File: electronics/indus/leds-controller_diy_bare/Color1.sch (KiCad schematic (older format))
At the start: 17 parts

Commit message: wip bare diy controller - dcdc and refactor
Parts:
- gave numbers to parts that had none: 17
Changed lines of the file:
@@
 $Descr A4 11693 8268
 encoding utf-8
-Sheet 4 8
+Sheet 4 9
 Title "Carte controlleur de LEDs 4 canaux"
 Date ""
@@
 VIN
 $Comp
-L TPS92513 U?
+L TPS92513 U4
 U 1 1 57155637
 P 5800 3550
-F 0 "U?" H 6150 2600 60  0000 C CNN
+F 0 "U4" H 6150 2600 60  0000 C CNN
 F 1 "TPS92513" H 5400 2600 60  0000 C CNN
 F 2 "" H 5950 3650 60  0000 C CNN
@@
 $EndComp
 $Comp
-L C-RESCUE-leds-controller C?
+L C-RESCUE-leds-controller C14
 U 1 1 5715571A
 P 1600 4150
-F 0 "C?" H 1600 4250 40  0000 L CNN
+F 0 "C14" H 1600 4250 40  0000 L CNN
 F 1 "C" H 1606 4065 40  0000 L CNN
 F 2 "" H 1638 4000 30  0000 C CNN
@@
 $EndComp
 $Comp
-L GND-RESCUE-leds-controller #PWR?
+L GND-RESCUE-leds-controller #PWR019
 U 1 1 571557B2
 P 5950 5250
-F 0 "#PWR?" H 5950 5250 30  0001 C CNN
+F 0 "#PWR019" H 5950 5250 30  0001 C CNN
 F 1 "GND" H 5950 5180 30  0001 C CNN
 F 2 "" H 5950 5250 60  0000 C CNN
@@
 $EndComp
 $Comp
-L R-RESCUE-leds-controller R?
+L R-RESCUE-leds-controller R15
 U 1 1 571557E1
 P 2150 3800
-F 0 "R?" V 2230 3800 40  0000 C CNN
+F 0 "R15" V 2230 3800 40  0000 C CNN
 F 1 "R" V 2157 3801 40  0000 C CNN
 F 2 "" V 2080 3800 30  0000 C CNN
@@
 $EndComp
 $Comp
-L R-RESCUE-leds-controller R?
+L R-RESCUE-leds-controller R16
 U 1 1 5715580E
 P 2150 4500
-F 0 "R?" V 2230 4500 40  0000 C CNN
+F 0 "R16" V 2230 4500 40  0000 C CNN
 F 1 "R" V 2157 4501 40  0000 C CNN
 F 2 "" V 2080 4500 30  0000 C CNN
@@
 $EndComp
 $Comp
-L C-RESCUE-leds-controller C?
+L C-RESCUE-leds-controller C15
 U 1 1 5715589F
 P 3050 4300
-F 0 "C?" H 3050 4400 40  0000 L CNN
+F 0 "C15" H 3050 4400 40  0000 L CNN
 F 1 "C" H 3056 4215 40  0000 L CNN
 F 2 "" H 3088 4150 30  0000 C CNN
@@
 $EndComp
 $Comp
-L R-RESCUE-leds-controller R?
+L R-RESCUE-leds-controller R17
 U 1 1 571558C4
 P 4050 4500
-F 0 "R?" V 4130 4500 40  0000 C CNN
+F 0 "R17" V 4130 4500 40  0000 C CNN
 F 1 "R" V 4057 4501 40  0000 C CNN
 F 2 "" V 3980 4500 30  0000 C CNN
@@
 $EndComp
 $Comp
-L INDUCTOR L?
+L INDUCTOR L3
 U 1 1 57155F0C
 P 8200 3450
-F 0 "L?" V 8150 3450 40  0000 C CNN
+F 0 "L3" V 8150 3450 40  0000 C CNN
 F 1 "XAL6060-153MEC - 15µH - 6A" V 8300 3450 40  0000 C CNN
 F 2 "risebox:SELF_COILCRAFT_XAL6060-153" H 8200 3450 60  0001 C CNN
@@
 self métallique
 $Comp
-L C-RESCUE-leds-controller C?
+L C-RESCUE-leds-controller C16
 U 1 1 571560D6
 P 6800 2900
-F 0 "C?" H 6800 3000 40  0000 L CNN
+F 0 "C16" H 6800 3000 40  0000 L CNN
 F 1 "C" H 6806 2815 40  0000 L CNN
 F 2 "" H 6838 2750 30  0000 C CNN
@@
 $EndComp
 $Comp
-L C-RESCUE-leds-controller C?
+L C-RESCUE-leds-controller C17
 U 1 1 57156549
 P 9550 3750
-F 0 "C?" H 9550 3850 40  0000 L CNN
+F 0 "C17" H 9550 3850 40  0000 L CNN
 F 1 "C" H 9556 3665 40  0000 L CNN
 F 2 "" H 9588 3600 30  0000 C CNN
@@
 $EndComp
 $Comp
-L R-RESCUE-leds-controller R?
+L R-RESCUE-leds-controller R18
 U 1 1 5715662A
 P 8200 4050
-F 0 "R?" V 8280 4050 40  0000 C CNN
+F 0 "R18" V 8280 4050 40  0000 C CNN
 F 1 "R" V 8207 4051 40  0000 C CNN
 F 2 "" V 8130 4050 30  0000 C CNN
@@
 $EndComp
 $Comp
-L R-RESCUE-leds-controller R?
+L R-RESCUE-leds-controller R19
 U 1 1 57156725
 P 10150 4500
-F 0 "R?" V 10230 4500 40  0000 C CNN
+F 0 "R19" V 10230 4500 40  0000 C CNN
 F 1 "R" V 10157 4501 40  0000 C CNN
 F 2 "" V 10080 4500 30  0000 C CNN
@@
 $EndComp
 $Comp
-L DIODESCH D?
+L DIODESCH D4
 U 1 1 57156848
 P 7350 4500
-F 0 "D?" H 7350 4600 40  0000 C CNN
+F 0 "D4" H 7350 4600 40  0000 C CNN
 F 1 "DIODESCH" H 7350 4400 40  0000 C CNN
 F 2 "" H 7350 4500 60  0000 C CNN
@@
 PDIM
 $Comp
-L JUMPER JP?
+L JUMPER JP1
 U 1 1 5760B831
 P 2400 1000
-F 0 "JP?" H 2400 1150 50  0000 C CNN
+F 0 "JP1" H 2400 1150 50  0000 C CNN
 F 1 "JUMPER" H 2400 920 50  0000 C CNN
 F 2 "" H 2400 1000 50  0000 C CNN
@@
 $EndComp
 $Comp
-L JUMPER JP?
+L JUMPER JP2
 U 1 1 5760B8E2
 P 2400 1350
-F 0 "JP?" H 2400 1500 50  0000 C CNN
+F 0 "JP2" H 2400 1500 50  0000 C CNN
 F 1 "JUMPER" H 2400 1270 50  0000 C CNN
 F 2 "" H 2400 1350 50  0000 C CNN
@@
 $EndComp
 $Comp
-L JUMPER JP?
+L JUMPER JP3
 U 1 1 5760B931
 P 2400 1700
-F 0 "JP?" H 2400 1850 50  0000 C CNN
+F 0 "JP3" H 2400 1850 50  0000 C CNN
 F 1 "JUMPER" H 2400 1620 50  0000 C CNN
 F 2 "" H 2400 1700 50  0000 C CNN
@@
 $EndComp
 $Comp
-L JUMPER JP?
+L JUMPER JP4
 U 1 1 5760B986
 P 2400 2050
-F 0 "JP?" H 2400 2200 50  0000 C CNN
+F 0 "JP4" H 2400 2200 50  0000 C CNN
 F 1 "JUMPER" H 2400 1970 50  0000 C CNN
 F 2 "" H 2400 2050 50  0000 C CNN
@@
 REG_0.35A
 $Comp
-L JUMPER JP?
+L JUMPER JP5
 U 1 1 5760BC5B
 P 5650 1450
-F 0 "JP?" H 5650 1600 50  0000 C CNN
+F 0 "JP5" H 5650 1600 50  0000 C CNN
 F 1 "JUMPER" H 5650 1370 50  0000 C CNN
 F 2 "" H 5650 1450 50  0000 C CNN

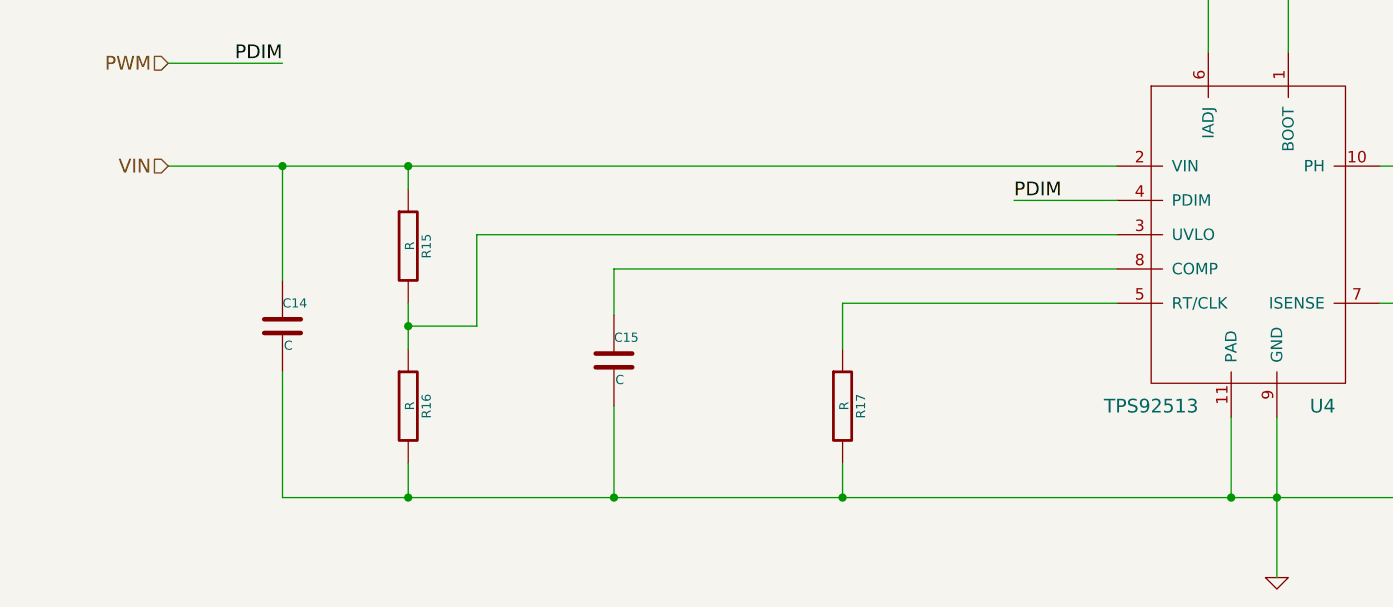
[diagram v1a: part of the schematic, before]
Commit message: schema done - misses values
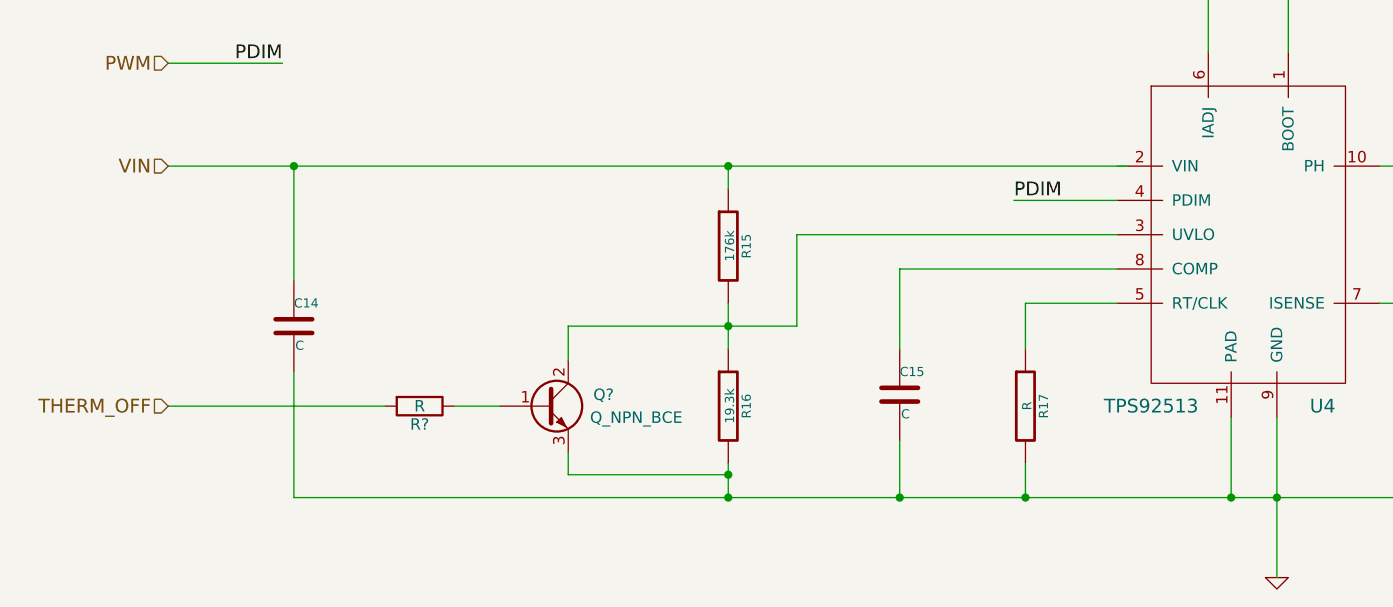
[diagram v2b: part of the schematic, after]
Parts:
- added Q?: Q_NPN_BCE, symbol Q_NPN_BCE
- added R?: R, symbol R
- R15: value R -> 176k
- R16: value R -> 19.3k
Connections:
- net GND: now also Q?.3 (E)
- net VIN: no longer U4.2 (VIN)
- net at R15.2, R16.1, U4.3 (UVLO): now also Q?.2 (C)
- new net: Q?.1 (B), R?.1
- new net THERM_OFF: R?.2
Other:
- moved on the sheet: C14, C15, R15, R16, R17
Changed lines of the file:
@@
 $Descr A4 11693 8268
 encoding utf-8
-Sheet 4 9
+Sheet 3 9
 Title "Carte controlleur de LEDs 4 canaux"
 Date ""
@@
 L C-RESCUE-leds-controller C14
 U 1 1 5715571A
-P 1600 4150
-F 0 "C14" H 1600 4250 40  0000 L CNN
-F 1 "C" H 1606 4065 40  0000 L CNN
-F 2 "" H 1638 4000 30  0000 C CNN
-F 3 "" H 1600 4150 60  0000 C CNN
-	1    1600 4150
+P 1650 4150
+F 0 "C14" H 1650 4250 40  0000 L CNN
+F 1 "C" H 1656 4065 40  0000 L CNN
+F 2 "" H 1688 4000 30  0000 C CNN
+F 3 "" H 1650 4150 60  0000 C CNN
+	1    1650 4150
 	1    0    0    -1
 $EndComp
@@
 L R-RESCUE-leds-controller R15
 U 1 1 571557E1
-P 2150 3800
-F 0 "R15" V 2230 3800 40  0000 C CNN
-F 1 "R" V 2157 3801 40  0000 C CNN
-F 2 "" V 2080 3800 30  0000 C CNN
-F 3 "" H 2150 3800 30  0000 C CNN
-	1    2150 3800
+P 3550 3800
+F 0 "R15" V 3630 3800 40  0000 C CNN
+F 1 "176k" V 3557 3801 40  0000 C CNN
+F 2 "" V 3480 3800 30  0000 C CNN
+F 3 "" H 3550 3800 30  0000 C CNN
+	1    3550 3800
 	1    0    0    -1
 $EndComp
@@
 L R-RESCUE-leds-controller R16
 U 1 1 5715580E
-P 2150 4500
-F 0 "R16" V 2230 4500 40  0000 C CNN
-F 1 "R" V 2157 4501 40  0000 C CNN
-F 2 "" V 2080 4500 30  0000 C CNN
-F 3 "" H 2150 4500 30  0000 C CNN
-	1    2150 4500
+P 3550 4500
+F 0 "R16" V 3630 4500 40  0000 C CNN
+F 1 "19.3k" V 3557 4501 40  0000 C CNN
+F 2 "" V 3480 4500 30  0000 C CNN
+F 3 "" H 3550 4500 30  0000 C CNN
+	1    3550 4500
 	1    0    0    -1
 $EndComp
@@
 L C-RESCUE-leds-controller C15
 U 1 1 5715589F
-P 3050 4300
-F 0 "C15" H 3050 4400 40  0000 L CNN
-F 1 "C" H 3056 4215 40  0000 L CNN
-F 2 "" H 3088 4150 30  0000 C CNN
-F 3 "" H 3050 4300 60  0000 C CNN
-	1    3050 4300
+P 4300 4450
+F 0 "C15" H 4300 4550 40  0000 L CNN
+F 1 "C" H 4306 4365 40  0000 L CNN
+F 2 "" H 4338 4300 30  0000 C CNN
+F 3 "" H 4300 4450 60  0000 C CNN
+	1    4300 4450
 	1    0    0    -1
 $EndComp
@@
 L R-RESCUE-leds-controller R17
 U 1 1 571558C4
-P 4050 4500
-F 0 "R17" V 4130 4500 40  0000 C CNN
-F 1 "R" V 4057 4501 40  0000 C CNN
-F 2 "" V 3980 4500 30  0000 C CNN
-F 3 "" H 4050 4500 30  0000 C CNN
-	1    4050 4500
+P 4850 4500
+F 0 "R17" V 4930 4500 40  0000 C CNN
+F 1 "R" V 4857 4501 40  0000 C CNN
+F 2 "" V 4780 4500 30  0000 C CNN
+F 3 "" H 4850 4500 30  0000 C CNN
+	1    4850 4500
 	1    0    0    -1
 $EndComp
@@
 	0    1    1    0
 $EndComp
-Wire Wire Line
-	1100 3450 1600 3450
-Wire Wire Line
-	1600 3450 2150 3450
-Wire Wire Line
-	2150 3450 5250 3450
-Wire Wire Line
-	1600 3950 1600 3450
-Connection ~ 1600 3450
-Wire Wire Line
-	1600 4350 1600 4900
-Wire Wire Line
-	1600 4900 2150 4900
-Wire Wire Line
-	2150 4900 3050 4900
-Wire Wire Line
-	3050 4900 4050 4900
-Wire Wire Line
-	4050 4900 5750 4900
-Wire Wire Line
-	5750 4900 5950 4900
-Wire Wire Line
-	5950 4900 7350 4900
-Wire Wire Line
-	7350 4900 10150 4900
-Wire Wire Line
-	5950 4550 5950 4900
-Wire Wire Line
-	5950 4900 5950 5250
-Wire Wire Line
-	5750 4550 5750 4900
-Connection ~ 5750 4900
-Connection ~ 5950 4900
-Wire Wire Line
-	2150 3550 2150 3450
-Connection ~ 2150 3450
-Wire Wire Line
-	2150 4050 2150 4150
-Wire Wire Line
-	2150 4150 2150 4250
-Wire Wire Line
-	2150 4750 2150 4900
-Connection ~ 2150 4900
-Wire Wire Line
-	2150 4150 2450 4150
-Wire Wire Line
-	2450 4150 2450 3750
-Wire Wire Line
-	2450 3750 5250 3750
-Connection ~ 2150 4150
-Wire Wire Line
-	3050 4500 3050 4900
-Connection ~ 3050 4900
-Wire Wire Line
-	3050 4100 3050 3900
-Wire Wire Line
-	3050 3900 5250 3900
-Wire Wire Line
-	5250 4050 4050 4050
-Wire Wire Line
-	4050 4050 4050 4250
-Wire Wire Line
-	4050 4750 4050 4900
-Connection ~ 4050 4900
-Wire Notes Line
-	7800 3650 8650 3650
-Wire Notes Line
-	8650 3100 7800 3100
-Wire Notes Line
-	7800 3100 7800 3200
-Wire Notes Line
-	7800 3650 7800 3550
-Wire Notes Line
-	8650 3650 8650 3550
-Wire Notes Line
-	8650 3100 8650 3200
-Wire Wire Line
-	6400 3450 6800 3450
-Wire Wire Line
-	6800 3450 7350 3450
-Wire Wire Line
-	7350 3450 7900 3450
-Wire Wire Line
-	6000 2950 6000 2250
-Wire Wire Line
-	6000 2250 6800 2250
-Wire Wire Line
-	6800 2250 6800 2700
-Wire Wire Line
-	6800 3100 6800 3450
-Connection ~ 6800 3450
-Wire Wire Line
-	8500 3450 9550 3450
-Wire Wire Line
-	9550 3450 10450 3450
-Wire Wire Line
-	9550 3550 9550 3450
-Connection ~ 9550 3450
-Wire Wire Line
-	9550 3950 9550 4050
-Connection ~ 9550 4050
-Wire Wire Line
-	6400 4050 7950 4050
-Wire Wire Line
-	8450 4050 9550 4050
-Wire Wire Line
-	9550 4050 10150 4050
-Wire Wire Line
-	10150 4050 10450 4050
-Wire Wire Line
-	10150 4250 10150 4050
-Connection ~ 10150 4050
-Wire Wire Line
-	10150 4900 10150 4750
-Wire Wire Line
-	7350 4300 7350 3450
-Connection ~ 7350 3450
-Wire Wire Line
-	7350 4700 7350 4900
-Connection ~ 7350 4900
-Wire Wire Line
-	1100 3000 1600 3000
-Wire Wire Line
-	5250 3600 4800 3600
-Wire Wire Line
-	1100 1000 2100 1000
-Wire Wire Line
-	1100 1350 2100 1350
-Wire Wire Line
-	1100 1700 2100 1700
-Wire Wire Line
-	1100 2050 2100 2050
-Wire Wire Line
-	2700 1000 3950 1000
-Wire Wire Line
-	3950 1000 5650 1000
-Wire Wire Line
-	5650 1000 10450 1000
-Wire Wire Line
-	2700 1350 3950 1350
-Wire Wire Line
-	3950 1000 3950 1350
-Wire Wire Line
-	3950 1350 3950 1700
-Wire Wire Line
-	3950 1700 3950 2050
-Connection ~ 3950 1000
-Wire Wire Line
-	3950 1700 2700 1700
-Connection ~ 3950 1350
-Wire Wire Line
-	3950 2050 2700 2050
-Connection ~ 3950 1700
-Connection ~ 5650 1000
-Wire Wire Line
-	5650 1950 10450 1950
-Connection ~ 5650 1950
-Wire Wire Line
-	5650 1750 5650 1950
-Wire Wire Line
-	5650 1950 5650 2950
-Wire Wire Line
-	5650 1150 5650 1000
 Text HLabel 10450 1000 2    60   Output ~ 0
 POT_IN
 Text HLabel 10450 1950 2    60   Output ~ 0
 POT_OUT
+Wire Wire Line
+	1100 3450 1650 3450
+Wire Wire Line
+	1650 3450 3550 3450
+Wire Wire Line
+	3550 3450 3550 3450
+Wire Wire Line
+	3550 3450 5300 3450
+Wire Wire Line
+	1650 4900 3550 4900
+Wire Wire Line
+	3550 4900 4300 4900
+Wire Wire Line
+	4300 4900 4850 4900
+Wire Wire Line
+	4850 4900 5750 4900
+Wire Wire Line
+	5750 4900 5950 4900
+Wire Wire Line
+	5950 4900 7350 4900
+Wire Wire Line
+	7350 4900 10150 4900
+Wire Wire Line
+	5950 4550 5950 4900
+Wire Wire Line
+	5950 4900 5950 5250
+Wire Wire Line
+	5750 4550 5750 4900
+Connection ~ 5750 4900
+Connection ~ 5950 4900
+Wire Wire Line
+	3550 4050 3550 4150
+Wire Wire Line
+	3550 4150 3550 4250
+Wire Wire Line
+	3850 4150 3850 3750
+Wire Wire Line
+	3850 3750 5250 3750
+Connection ~ 3550 4150
+Wire Wire Line
+	4300 4650 4300 4900
+Connection ~ 4300 4900
+Wire Wire Line
+	4300 4250 4300 3900
+Wire Wire Line
+	4300 3900 5250 3900
+Wire Wire Line
+	5250 4050 4850 4050
+Wire Wire Line
+	4850 4050 4850 4250
+Wire Wire Line
+	4850 4750 4850 4900
+Connection ~ 4850 4900
+Wire Notes Line
+	7800 3650 8650 3650
+Wire Notes Line
+	8650 3100 7800 3100
+Wire Notes Line
+	7800 3100 7800 3200
+Wire Notes Line
+	7800 3650 7800 3550
+Wire Notes Line
+	8650 3650 8650 3550
+Wire Notes Line
+	8650 3100 8650 3200
+Wire Wire Line
+	6400 3450 6800 3450
+Wire Wire Line
+	6800 3450 7350 3450
+Wire Wire Line
+	7350 3450 7900 3450
+Wire Wire Line
+	6000 2950 6000 2250
+Wire Wire Line
+	6000 2250 6800 2250
+Wire Wire Line
+	6800 2250 6800 2700
+Wire Wire Line
+	6800 3100 6800 3450
+Connection ~ 6800 3450
+Wire Wire Line
+	8500 3450 9550 3450
+Wire Wire Line
+	9550 3450 10450 3450
+Wire Wire Line
+	9550 3550 9550 3450
+Connection ~ 9550 3450
+Wire Wire Line
+	9550 3950 9550 4050
+Connection ~ 9550 4050
+Wire Wire Line
+	6400 4050 7950 4050
+Wire Wire Line
+	8450 4050 9550 4050
+Wire Wire Line
+	9550 4050 10150 4050
+Wire Wire Line
+	10150 4050 10450 4050
+Wire Wire Line
+	10150 4250 10150 4050
+Connection ~ 10150 4050
+Wire Wire Line
+	10150 4900 10150 4750
+Wire Wire Line
+	7350 4300 7350 3450
+Connection ~ 7350 3450
+Wire Wire Line
+	7350 4700 7350 4900
+Connection ~ 7350 4900
+Wire Wire Line
+	1100 3000 1600 3000
+Wire Wire Line
+	5250 3600 4800 3600
+Wire Wire Line
+	1100 1000 2100 1000
+Wire Wire Line
+	1100 1350 2100 1350
+Wire Wire Line
+	1100 1700 2100 1700
+Wire Wire Line
+	1100 2050 2100 2050
+Wire Wire Line
+	2700 1000 3950 1000
+Wire Wire Line
+	3950 1000 5650 1000
+Wire Wire Line
+	5650 1000 10450 1000
+Wire Wire Line
+	2700 1350 3950 1350
+Wire Wire Line
+	3950 1000 3950 1350
+Wire Wire Line
+	3950 1350 3950 1700
+Wire Wire Line
+	3950 1700 3950 2050
+Connection ~ 3950 1000
+Wire Wire Line
+	3950 1700 2700 1700
+Connection ~ 3950 1350
+Wire Wire Line
+	3950 2050 2700 2050
+Connection ~ 3950 1700
+Connection ~ 5650 1000
+Wire Wire Line
+	5650 1950 10450 1950
+Connection ~ 5650 1950
+Wire Wire Line
+	5650 1750 5650 1950
+Wire Wire Line
+	5650 1950 5650 2950
+Wire Wire Line
+	5650 1150 5650 1000
+Wire Wire Line
+	1650 3950 1650 3450
+Connection ~ 1650 3450
+Wire Wire Line
+	1650 4350 1650 4900
+Wire Wire Line
+	3550 4750 3550 4800
+Wire Wire Line
+	3550 4800 3550 4900
+Wire Wire Line
+	3550 3550 3550 3450
+Connection ~ 3550 3450
+Connection ~ 3550 4900
+Wire Wire Line
+	2850 4300 2850 4150
+Wire Wire Line
+	2850 4150 3550 4150
+Wire Wire Line
+	3550 4150 3850 4150
+Wire Wire Line
+	2850 4700 2850 4800
+Wire Wire Line
+	2850 4800 3550 4800
+Connection ~ 3550 4800
+$Comp
+L Q_NPN_BCE Q?
+U 1 1 5763D1F6
+P 2750 4500
+F 0 "Q?" H 3050 4550 50  0000 R CNN
+F 1 "Q_NPN_BCE" H 3350 4450 50  0000 R CNN
+F 2 "" H 2950 4600 50  0000 C CNN
+F 3 "" H 2750 4500 50  0000 C CNN
+	1    2750 4500
+	1    0    0    -1
+$EndComp
+Text HLabel 1100 4500 0    60   Input ~ 0
+THERM_OFF
+$Comp
+L R R?
+U 1 1 5763D8FD
+P 2200 4500
+F 0 "R?" V 2280 4500 50  0000 C CNN
+F 1 "R" V 2200 4500 50  0000 C CNN
+F 2 "" V 2130 4500 50  0000 C CNN
+F 3 "" H 2200 4500 50  0000 C CNN
+	1    2200 4500
+	0    1    1    0
+$EndComp
+Wire Wire Line
+	2350 4500 2550 4500
+Wire Wire Line
+	2050 4500 1100 4500
 $EndSCHEMATC

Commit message: schema prctically ok missing refs
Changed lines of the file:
@@
 POT_OUT
 Wire Wire Line
-	1100 3450 1650 3450
+	1100 3450 5300 3450
 Wire Wire Line
-	1650 3450 3550 3450
+	1650 4900 10150 4900
 Wire Wire Line
-	3550 3450 3550 3450
-Wire Wire Line
-	3550 3450 5300 3450
-Wire Wire Line
-	1650 4900 3550 4900
-Wire Wire Line
-	3550 4900 4300 4900
-Wire Wire Line
-	4300 4900 4850 4900
-Wire Wire Line
-	4850 4900 5750 4900
-Wire Wire Line
-	5750 4900 5950 4900
-Wire Wire Line
-	5950 4900 7350 4900
-Wire Wire Line
-	7350 4900 10150 4900
-Wire Wire Line
-	5950 4550 5950 4900
-Wire Wire Line
-	5950 4900 5950 5250
+	5950 4550 5950 5250
 Wire Wire Line
 	5750 4550 5750 4900
@@
 Connection ~ 5950 4900
 Wire Wire Line
-	3550 4050 3550 4150
-Wire Wire Line
-	3550 4150 3550 4250
+	3550 4050 3550 4250
 Wire Wire Line
 	3850 4150 3850 3750
@@
 	8650 3100 8650 3200
 Wire Wire Line
-	6400 3450 6800 3450
-Wire Wire Line
-	6800 3450 7350 3450
-Wire Wire Line
-	7350 3450 7900 3450
+	6400 3450 7900 3450
 Wire Wire Line
 	6000 2950 6000 2250
@@
 Connection ~ 6800 3450
 Wire Wire Line
-	8500 3450 9550 3450
-Wire Wire Line
-	9550 3450 10450 3450
+	8500 3450 10450 3450
 Wire Wire Line
 	9550 3550 9550 3450
@@
 	6400 4050 7950 4050
 Wire Wire Line
-	8450 4050 9550 4050
-Wire Wire Line
-	9550 4050 10150 4050
-Wire Wire Line
-	10150 4050 10450 4050
+	8450 4050 10450 4050
 Wire Wire Line
 	10150 4250 10150 4050
@@
 	1100 2050 2100 2050
 Wire Wire Line
-	2700 1000 3950 1000
-Wire Wire Line
-	3950 1000 5650 1000
-Wire Wire Line
-	5650 1000 10450 1000
+	2700 1000 10450 1000
 Wire Wire Line
 	2700 1350 3950 1350
 Wire Wire Line
-	3950 1000 3950 1350
-Wire Wire Line
-	3950 1350 3950 1700
-Wire Wire Line
-	3950 1700 3950 2050
+	3950 1000 3950 2050
 Connection ~ 3950 1000
 Wire Wire Line
@@
 Connection ~ 5650 1950
 Wire Wire Line
-	5650 1750 5650 1950
-Wire Wire Line
-	5650 1950 5650 2950
+	5650 1750 5650 2950
 Wire Wire Line
 	5650 1150 5650 1000
@@
 	1650 4350 1650 4900
 Wire Wire Line
-	3550 4750 3550 4800
-Wire Wire Line
-	3550 4800 3550 4900
+	3550 4750 3550 4900
 Wire Wire Line
 	3550 3550 3550 3450
@@
 	2850 4300 2850 4150
 Wire Wire Line
-	2850 4150 3550 4150
-Wire Wire Line
-	3550 4150 3850 4150
+	2850 4150 3850 4150
 Wire Wire Line
 	2850 4700 2850 4800

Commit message: schema prctically ok missing refs
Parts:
- gave numbers to parts that had none: 2
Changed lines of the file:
@@
 $EndComp
 $Comp
-L GND-RESCUE-leds-controller #PWR019
+L GND-RESCUE-leds-controller #PWR12
 U 1 1 571557B2
 P 5950 5250
-F 0 "#PWR019" H 5950 5250 30  0001 C CNN
+F 0 "#PWR12" H 5950 5250 30  0001 C CNN
 F 1 "GND" H 5950 5180 30  0001 C CNN
 F 2 "" H 5950 5250 60  0000 C CNN
@@
 Connection ~ 3550 4800
 $Comp
-L Q_NPN_BCE Q?
+L Q_NPN_BCE Q3
 U 1 1 5763D1F6
 P 2750 4500
-F 0 "Q?" H 3050 4550 50  0000 R CNN
+F 0 "Q3" H 3050 4550 50  0000 R CNN
 F 1 "Q_NPN_BCE" H 3350 4450 50  0000 R CNN
 F 2 "" H 2950 4600 50  0000 C CNN
@@
 THERM_OFF
 $Comp
-L R R?
+L R R12
 U 1 1 5763D8FD
 P 2200 4500
-F 0 "R?" V 2280 4500 50  0000 C CNN
+F 0 "R12" V 2280 4500 50  0000 C CNN
 F 1 "R" V 2200 4500 50  0000 C CNN
 F 2 "" V 2130 4500 50  0000 C CNN

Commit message: bom refs etc
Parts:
- JP1, JP2, JP3, JP4, JP5: value JUMPER -> M20-9990246
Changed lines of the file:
@@
 P 2400 1000
 F 0 "JP1" H 2400 1150 50  0000 C CNN
-F 1 "JUMPER" H 2400 920 50  0000 C CNN
+F 1 "M20-9990246" H 2400 920 50  0000 C CNN
 F 2 "" H 2400 1000 50  0000 C CNN
 F 3 "" H 2400 1000 50  0000 C CNN
@@
 P 2400 1350
 F 0 "JP2" H 2400 1500 50  0000 C CNN
-F 1 "JUMPER" H 2400 1270 50  0000 C CNN
+F 1 "M20-9990246" H 2400 1270 50  0000 C CNN
 F 2 "" H 2400 1350 50  0000 C CNN
 F 3 "" H 2400 1350 50  0000 C CNN
@@
 P 2400 1700
 F 0 "JP3" H 2400 1850 50  0000 C CNN
-F 1 "JUMPER" H 2400 1620 50  0000 C CNN
+F 1 "M20-9990246" H 2400 1620 50  0000 C CNN
 F 2 "" H 2400 1700 50  0000 C CNN
 F 3 "" H 2400 1700 50  0000 C CNN
@@
 P 2400 2050
 F 0 "JP4" H 2400 2200 50  0000 C CNN
-F 1 "JUMPER" H 2400 1970 50  0000 C CNN
+F 1 "M20-9990246" H 2400 1970 50  0000 C CNN
 F 2 "" H 2400 2050 50  0000 C CNN
 F 3 "" H 2400 2050 50  0000 C CNN
@@
 P 5650 1450
 F 0 "JP5" H 5650 1600 50  0000 C CNN
-F 1 "JUMPER" H 5650 1370 50  0000 C CNN
+F 1 "M20-9990246" H 5650 1370 50  0000 C CNN
 F 2 "" H 5650 1450 50  0000 C CNN
 F 3 "" H 5650 1450 50  0000 C CNN
